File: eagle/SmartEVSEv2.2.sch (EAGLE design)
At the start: 73 parts, among them CON1 3.5MM_12PIN, CON3 JST_10PIN_FFC, IC1 AOZ1280CI, IC2 LM7332MA, IC3 MCP9700A, IC4 PIC18F26K22-I/SOSSOP, IC5 SN65HVD72, IC6 FAN3214TMX, IC7 TC7660S, K1 AQH1213AX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

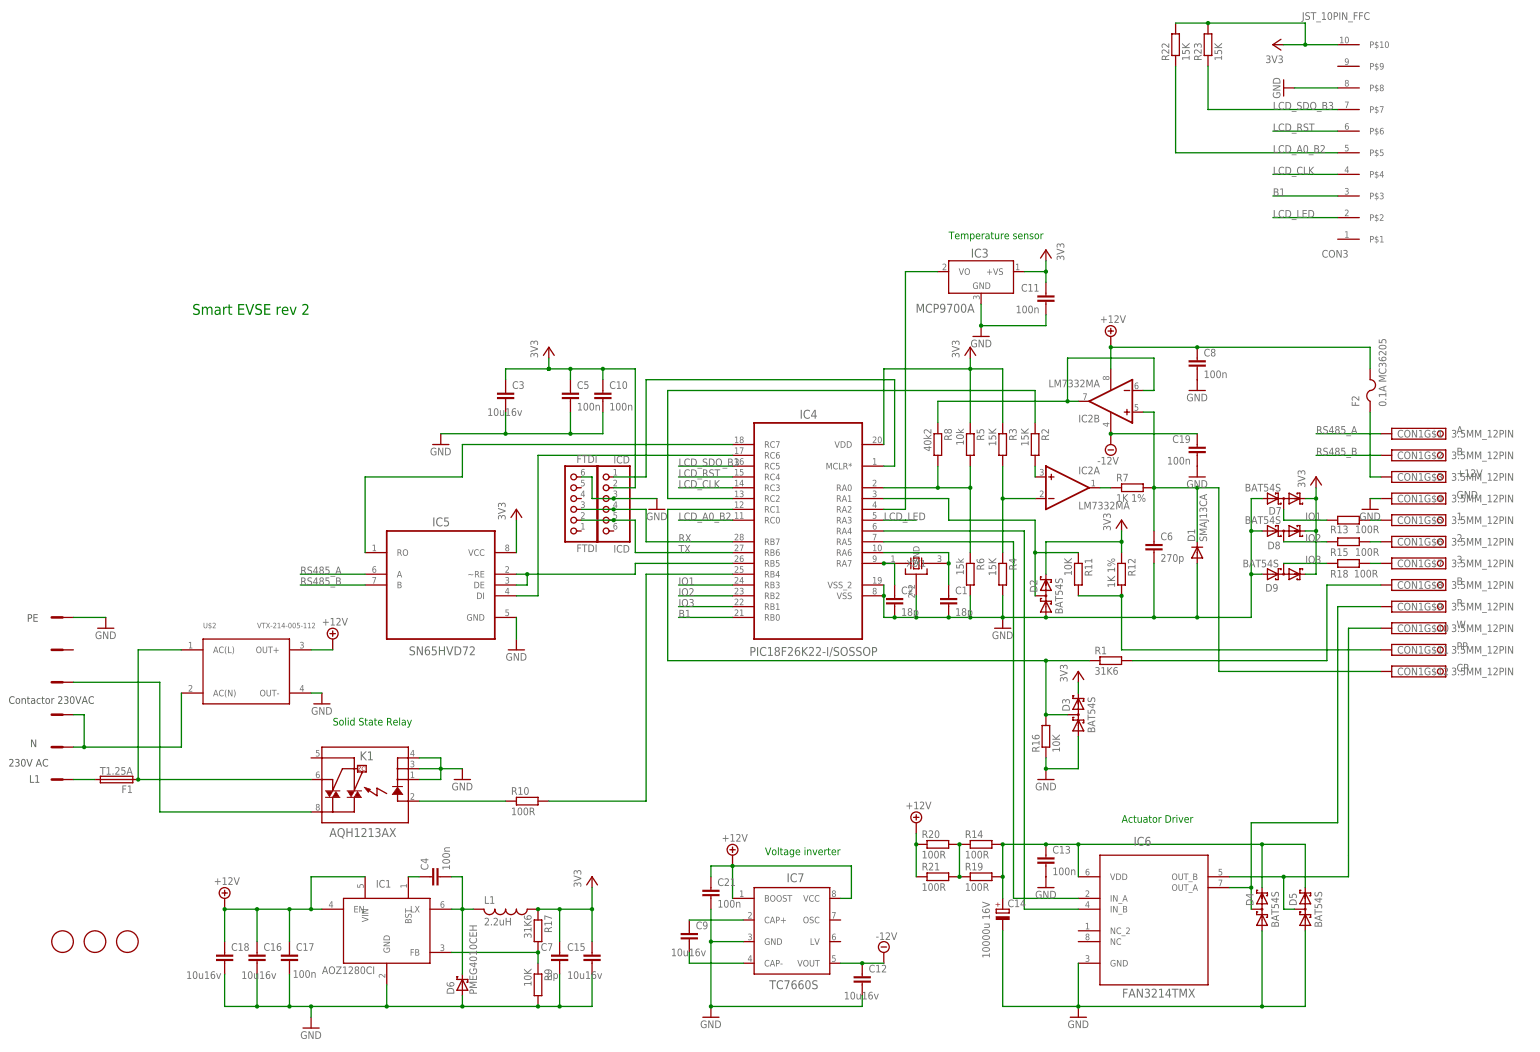
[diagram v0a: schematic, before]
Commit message: Updated Schematics
Updated schematic and board to version 2.2
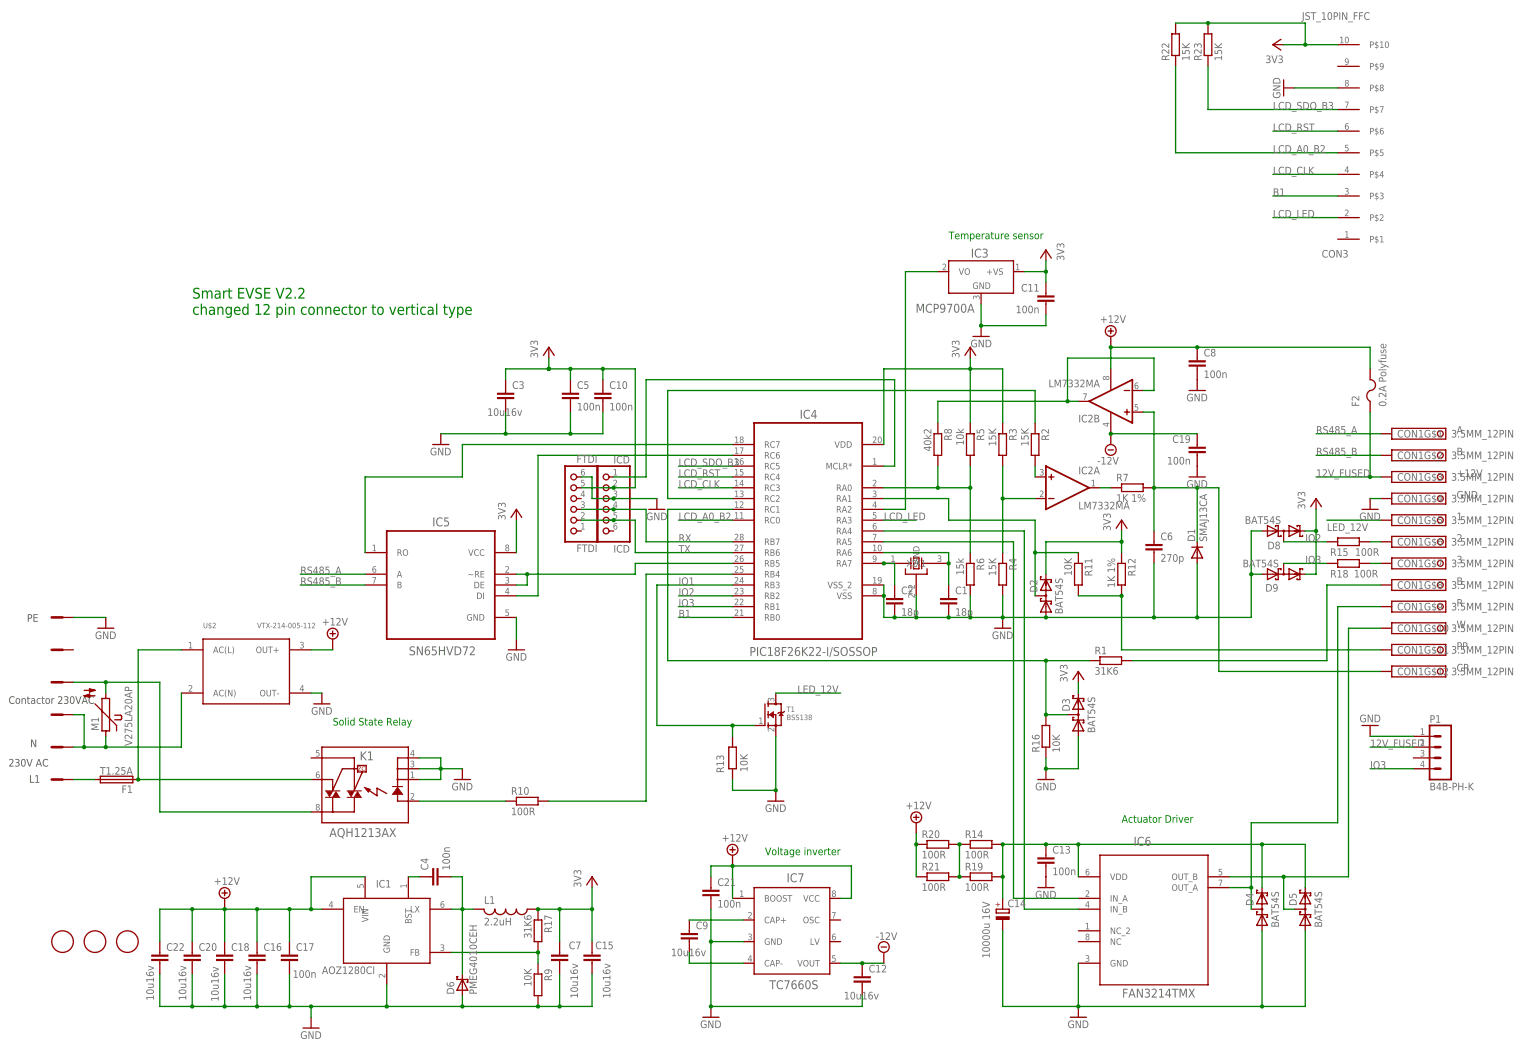
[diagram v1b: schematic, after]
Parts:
- removed D7: BAT54S, diode:BAT54S
- added C20, C22: 10u16v, rcl:C-EUC0805
- added M1: V275LA20AP, varistor:S14K40
- added P1: B4B-PH-K, con-jst-ph:B4B-PH-K
- added T1: BSS138, adafruit:MOSFET-NREFLOW
- C1, C10, C11, C13, C17, C19, C2, C21, C4, C5, C8: device rcl:C-EUC0805 -> rcl:C-EUC0603
- C12, C15, C16, C18, C3, C9: device rcl:C-EUC1206 -> rcl:C-EUC0805
- C7: value np -> 10u16v; device rcl:C-EUC1206 -> rcl:C-EUC0805
- CON2: value AST027-06 -> DG128-7.5
- F2: value 0.1A MC36205 -> 0.2A Polyfuse; device adafruit:PTCFUSE-1812 -> adafruit:PTCFUSE-1210
- R13: value 100R -> 10K
- renumbered X2 to CON2
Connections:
- removed net N$31: CON1G$3.K, F2.1
- removed net N$4: CON1G$5.K, R13.2
- new net 12V_FUSED: CON1G$3.K, F2.1, P1.2
- new net LED_12V: CON1G$5.K, T1.D
- net +12V: now also C20.1, C22.1
- net GND: now also C20.2, C22.2, P1.1, R13.1, T1.S; no longer D7.A1
- net IO1: now also R13.2, T1.G; no longer D7.C1A2, R13.1
- net IO3: now also P1.4
- net N$23: now also M1.2
- net N$26: now also M1.1
- net VCC: now also FTDI.5; no longer D7.C2
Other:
- note added: "Smart EVSE V2.2 changed 12 pin connector to vertical type"
- note removed: "Smart EVSE rev 2"
- moved on the sheet: R13
